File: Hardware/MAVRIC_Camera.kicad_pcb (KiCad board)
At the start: 2 copper layers, 7 parts, among them J1 MASTER, J2 CAMERA, J3 SERVO

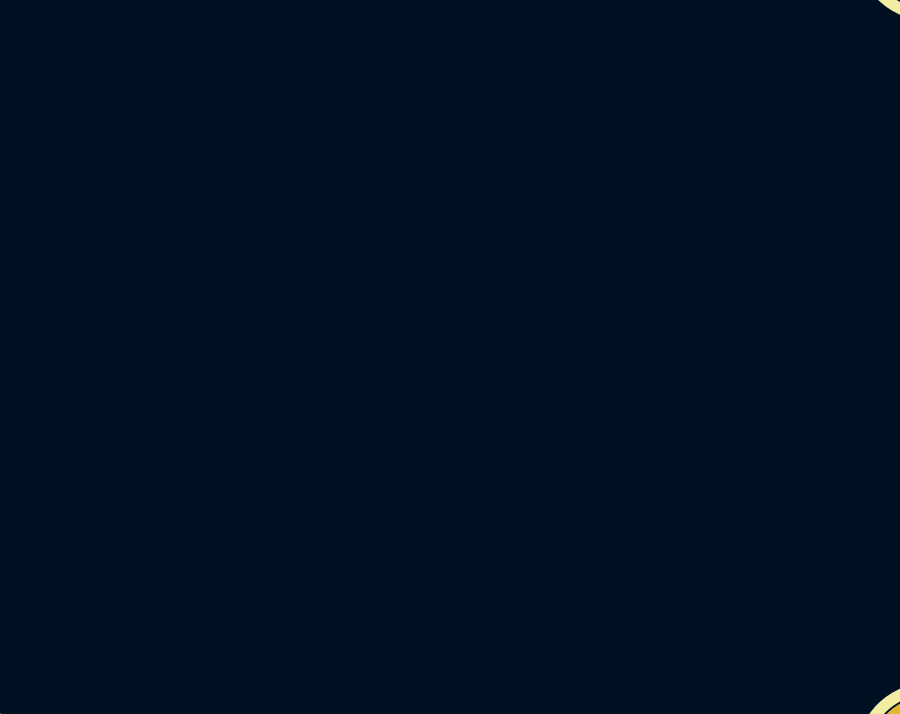
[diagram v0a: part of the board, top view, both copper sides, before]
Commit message: Add Dynamixel servo interface
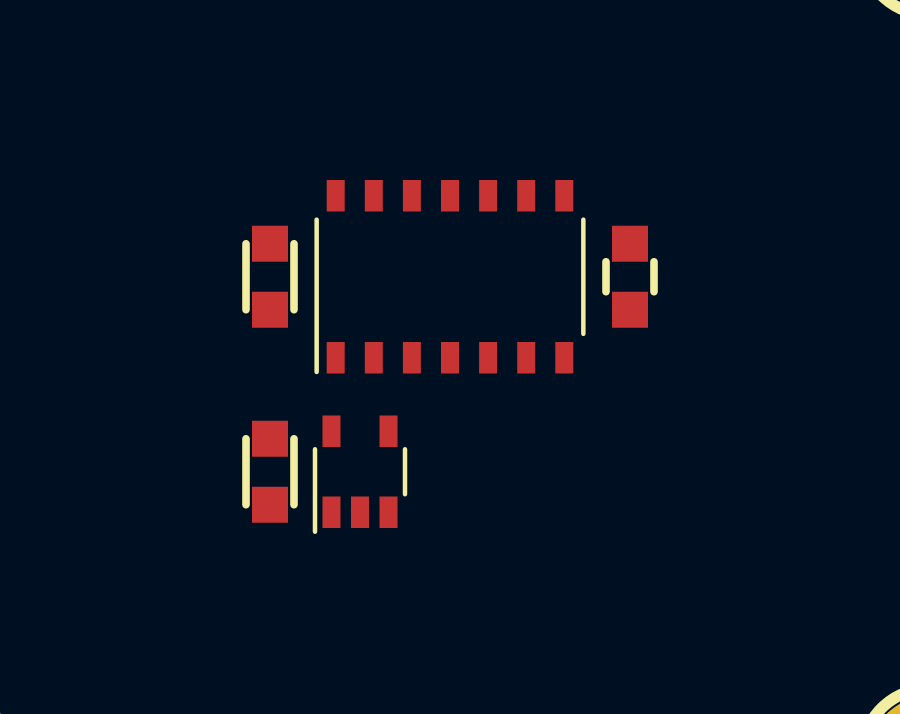
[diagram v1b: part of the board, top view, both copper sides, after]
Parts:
- added C1: 0.1uF, CAPC2012, F.Cu at (161.0, 111.0)
- added C2: 0.1uF, CAPC2012, F.Cu at (161.0, 117.5)
- added R1: 10k, RESC2012, F.Cu at (173.0, 111.0)
- added U1: SN74HC126, SOIC127P600-14N, F.Cu at (167.0, 111.0)
- added U2: SN74LVC1G04, SOT95P280-5N, F.Cu at (164.0, 117.5)
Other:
- net class Default: clearance 0.254 -> 0.2032; trace_width 0.254 -> 0.2032
- rule trace_clearance: 0.254 -> 0.2032
- rule trace_min: 0.254 -> 0.2032
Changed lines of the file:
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@@
 (kicad_pcb (version 3) (host pcbnew "(2013-07-07 BZR 4022)-stable")
   (general
-    (links 0)
-    (no_connects 0)
-    (area 147.269499 88.399999 217.244501 138.600001)
+    (links 11)
+    (no_connects 11)
+    (area 0 0 0 0)
     (thickness 1.6)
     (drawings 1)
     (tracks 0)
     (zones 0)
-    (modules 7)
-    (nets 1)
+    (modules 12)
+    (nets 6)
   )
   (page A3)
@@
   )
   (setup
-    (last_trace_width 0.254)
-    (trace_clearance 0.254)
+    (last_trace_width 0.2032)
+    (trace_clearance 0.2032)
     (zone_clearance 0.508)
     (zone_45_only no)
-    (trace_min 0.254)
+    (trace_min 0.2032)
     (segment_width 0.2)
     (edge_width 0.1)
@@
     (mod_text_size 1 1)
     (mod_text_width 0.15)
-    (pad_size 3.23 2.7)
+    (pad_size 0.6 1.05)
     (pad_drill 0)
     (pad_to_mask_clearance 0)
@@
   )
   (net 0 "")
+  (net 1 +5V)
+  (net 2 /SerDat)
+  (net 3 /SevDr)
+  (net 4 GND)
+  (net 5 N-000007)
   (net_class Default "This is the default net class."
-    (clearance 0.254)
-    (trace_width 0.254)
+    (clearance 0.2032)
+    (trace_width 0.2032)
     (via_dia 0.889)
     (via_drill 0.635)
@@
     (uvia_drill 0.127)
     (add_net "")
+    (add_net +5V)
+    (add_net /SerDat)
+    (add_net /SevDr)
+    (add_net GND)
+    (add_net N-000007)
   )
   (module 1pin (layer F.Cu)
@@
     )
   )
+  (module RESC2012 (layer F.Cu)
+    (at 173 111 90)
+    (fp_text reference R1 (at 0 0 180) (layer F.SilkS) hide
+      (effects (font (size 1.524 1.524) (thickness 0.3048)))
+    )
+    (fp_text value 10k (at 0 2.1 90) (layer F.SilkS) hide
+      (effects (font (size 1.524 1.524) (thickness 0.3048)))
+    )
+    (fp_line (start -0.5 0.8) (end 0.5 0.8) (layer F.SilkS) (width 0.254))
+    (fp_line (start -0.5 -0.8) (end 0.5 -0.8) (layer F.SilkS) (width 0.254))
+    (pad 1 smd rect (at -1.1 0 90) (size 1.2 1.2)
+      (layers F.Cu F.Paste F.Mask)
+      (net 2 /SerDat)
+    )
+    (pad 2 smd rect (at 1.1 0 90) (size 1.2 1.2)
+      (layers F.Cu F.Paste F.Mask)
+      (net 1 +5V)
+    )
+  )
+  (module CAPC2012 (layer F.Cu)
+    (at 161 111 270)
+    (descr "Cap 0805e / 2012m")
+    (fp_text reference C1 (at 0 0 360) (layer F.SilkS) hide
+      (effects (font (size 1.524 1.524) (thickness 0.3048)))
+    )
+    (fp_text value 0.1uF (at 0 2.1 270) (layer F.SilkS) hide
+      (effects (font (size 1.524 1.524) (thickness 0.3048)))
+    )
+    (fp_line (start 1.1 -0.8) (end -1.1 -0.8) (layer F.SilkS) (width 0.254))
+    (fp_line (start -1.1 0.8) (end 1.1 0.8) (layer F.SilkS) (width 0.254))
+    (pad 1 smd rect (at -1.1 0 270) (size 1.2 1.2)
+      (layers F.Cu F.Paste F.Mask)
+      (net 1 +5V)
+    )
+    (pad 2 smd rect (at 1.1 0 270) (size 1.2 1.2)
+      (layers F.Cu F.Paste F.Mask)
+      (net 4 GND)
+    )
+  )
+  (module SOT95P280-5N (layer F.Cu)
+    (at 164 117.5)
+    (fp_text reference U2 (at 0 0) (layer F.SilkS) hide
+      (effects (font (size 1 1) (thickness 0.15)))
+    )
+    (fp_text value SN74LVC1G04 (at 2.25 0 90) (layer F.SilkS) hide
+      (effects (font (size 1 1) (thickness 0.15)))
+    )
+    (fp_line (start 1.5 -0.75) (end 1.5 0.75) (layer F.SilkS) (width 0.15))
+    (fp_line (start -1.5 -0.75) (end -1.5 2) (layer F.SilkS) (width 0.15))
+    (pad 1 smd rect (at -0.95 1.35) (size 0.6 1.05)
+      (layers F.Cu F.Paste F.Mask)
+    )
+    (pad 2 smd rect (at 0 1.35) (size 0.6 1.05)
+      (layers F.Cu F.Paste F.Mask)
+      (net 3 /SevDr)
+    )
+    (pad 3 smd rect (at 0.95 1.35) (size 0.6 1.05)
+      (layers F.Cu F.Paste F.Mask)
+      (net 4 GND)
+    )
+    (pad 4 smd rect (at 0.95 -1.35) (size 0.6 1.05)
+      (layers F.Cu F.Paste F.Mask)
+      (net 5 N-000007)
+    )
+    (pad 5 smd rect (at -0.95 -1.35) (size 0.6 1.05)
+      (layers F.Cu F.Paste F.Mask)
+      (net 1 +5V)
+    )
+  )
+  (module CAPC2012 (layer F.Cu)
+    (at 161 117.5 270)
+    (descr "Cap 0805e / 2012m")
+    (fp_text reference C2 (at 0 0 360) (layer F.SilkS) hide
+      (effects (font (size 1.524 1.524) (thickness 0.3048)))
+    )
+    (fp_text value 0.1uF (at 0 2.1 270) (layer F.SilkS) hide
+      (effects (font (size 1.524 1.524) (thickness 0.3048)))
+    )
+    (fp_line (start 1.1 -0.8) (end -1.1 -0.8) (layer F.SilkS) (width 0.254))
+    (fp_line (start -1.1 0.8) (end 1.1 0.8) (layer F.SilkS) (width 0.254))
+    (pad 1 smd rect (at -1.1 0 270) (size 1.2 1.2)
+      (layers F.Cu F.Paste F.Mask)
+      (net 1 +5V)
+    )
+    (pad 2 smd rect (at 1.1 0 270) (size 1.2 1.2)
+      (layers F.Cu F.Paste F.Mask)
+      (net 4 GND)
+    )
+  )
+  (module SOIC127P600-14N (layer F.Cu)
+    (at 167 111)
+    (fp_text reference U1 (at 0 0) (layer F.SilkS) hide
+      (effects (font (size 1 1) (thickness 0.15)))
+    )
+    (fp_text value SN74HC126 (at 5.715 0 90) (layer F.SilkS) hide
+      (effects (font (size 1 1) (thickness 0.15)))
+    )
+    (fp_line (start 4.445 -1.905) (end 4.445 1.905) (layer F.SilkS) (width 0.15))
+    (fp_line (start -4.445 -1.905) (end -4.445 3.175) (layer F.SilkS) (width 0.15))
+    (pad 1 smd rect (at -3.81 2.7) (size 0.6 1.05)
+      (layers F.Cu F.Paste F.Mask)
+      (net 3 /SevDr)
+    )
+    (pad 2 smd rect (at -2.54 2.7) (size 0.6 1.05)
+      (layers F.Cu F.Paste F.Mask)
+    )
+    (pad 3 smd rect (at -1.27 2.7) (size 0.6 1.05)
+      (layers F.Cu F.Paste F.Mask)
+      (net 2 /SerDat)
+    )
+    (pad 4 smd rect (at 0 2.7) (size 0.6 1.05)
+      (layers F.Cu F.Paste F.Mask)
+      (net 5 N-000007)
+    )
+    (pad 5 smd rect (at 1.27 2.7) (size 0.6 1.05)
+      (layers F.Cu F.Paste F.Mask)
+      (net 2 /SerDat)
+    )
+    (pad 6 smd rect (at 2.54 2.7) (size 0.6 1.05)
+      (layers F.Cu F.Paste F.Mask)
+    )
+    (pad 7 smd rect (at 3.81 2.7) (size 0.6 1.05)
+      (layers F.Cu F.Paste F.Mask)
+      (net 4 GND)
+    )
+    (pad 8 smd rect (at 3.81 -2.7) (size 0.6 1.05)
+      (layers F.Cu F.Paste F.Mask)
+    )
+    (pad 9 smd rect (at 2.54 -2.7) (size 0.6 1.05)
+      (layers F.Cu F.Paste F.Mask)
+    )
+    (pad 10 smd rect (at 1.27 -2.7) (size 0.6 1.05)
+      (layers F.Cu F.Paste F.Mask)
+    )
+    (pad 11 smd rect (at 0 -2.7) (size 0.6 1.05)
+      (layers F.Cu F.Paste F.Mask)
+    )
+    (pad 12 smd rect (at -1.27 -2.7) (size 0.6 1.05)
+      (layers F.Cu F.Paste F.Mask)
+    )
+    (pad 13 smd rect (at -2.54 -2.7) (size 0.6 1.05)
+      (layers F.Cu F.Paste F.Mask)
+    )
+    (pad 14 smd rect (at -3.81 -2.7) (size 0.6 1.05)
+      (layers F.Cu F.Paste F.Mask)
+      (net 1 +5V)
+    )
+  )

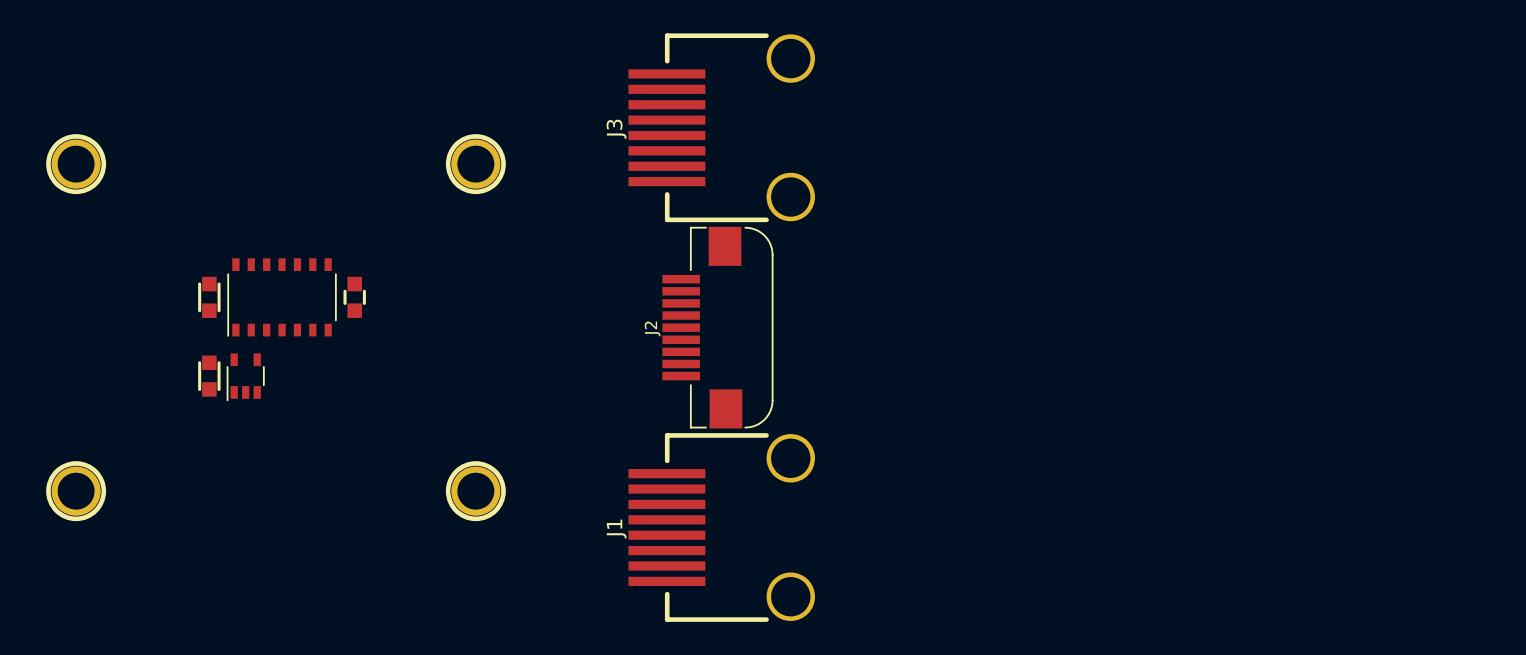
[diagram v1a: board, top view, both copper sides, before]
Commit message: Add servo power supply.
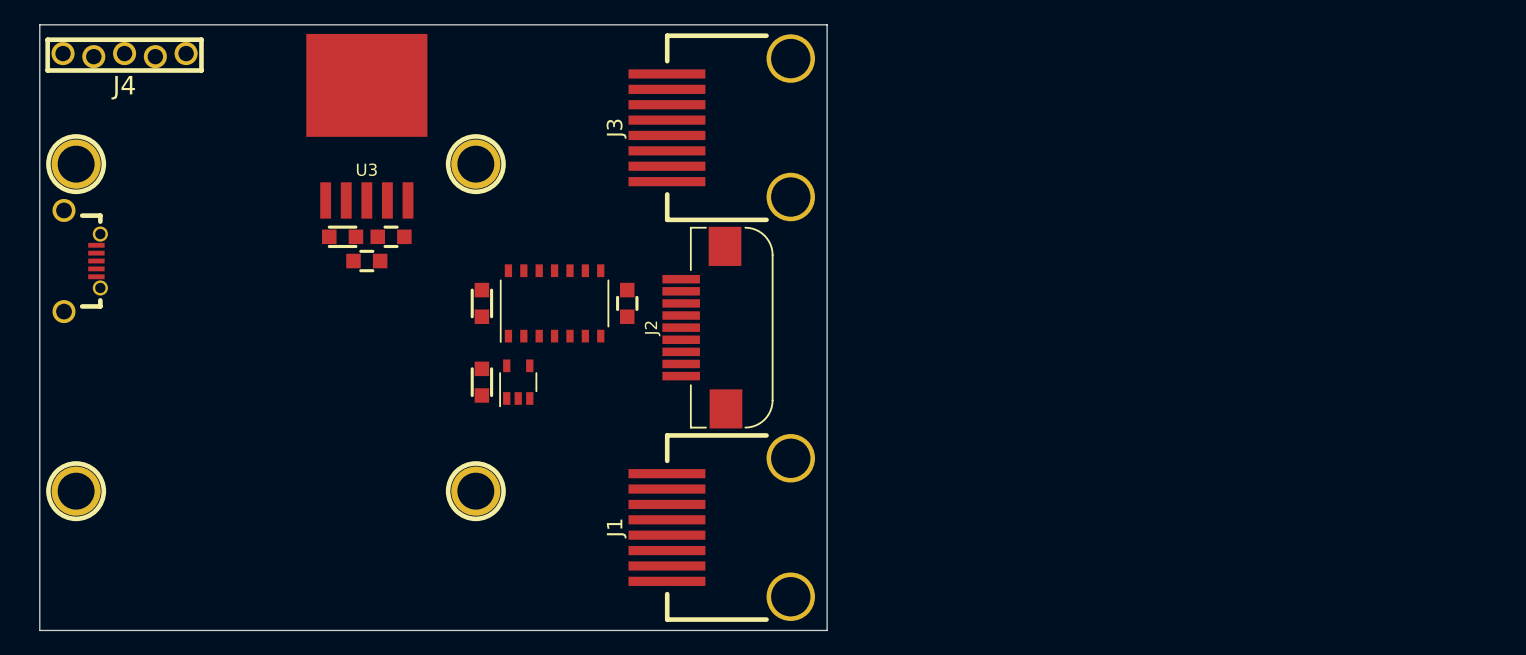
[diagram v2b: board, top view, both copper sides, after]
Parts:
- added C4: C, CAPC2012, F.Cu at (172.0, 106.0)
- added J4: ICSP-PIC, HDRV5W38P254_5X1-LOCK, F.Cu at (154.0, 91.0)
- added J5: USB, WM17143CT, F.Cu at (149.0, 108.0)
- added R2: R, RESC2012, F.Cu at (176.0, 106.0)
- added R3: R, RESC2012, F.Cu at (174.0, 108.0)
- added U3: BA00DD0W, TO263-6N, F.Cu at (174.0, 103.0)
- moved C1 22.5 mm to (183.5, 111.5)
- moved C2 22.5 mm to (183.5, 118.0)
- moved R1 22.5 mm to (195.5, 111.5)
- moved U1 22.5 mm to (189.5, 111.5)
- moved U2 22.5 mm to (186.5, 118.0)
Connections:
- J1 pad 4: (no net) -> +BATT
- J1 pad 5: (no net) -> +BATT
- J1 pad 7: (no net) -> GND
- J1 pad 8: (no net) -> GND
- J2 pad 3: (no net) -> GND
- J2 pad 5: (no net) -> GND
- J2 pad 7: (no net) -> GND
- J2 pad 9: (no net) -> GND
- J3 pad 1: (no net) -> /SevDat
- J3 pad 2: (no net) -> GND
- J3 pad 3: (no net) -> N-0000014
- J3 pad 4: (no net) -> N-0000014
- J3 pad 5: (no net) -> N-0000014
- J3 pad 6: (no net) -> N-0000014
- J3 pad 7: (no net) -> GND
- J3 pad 8: (no net) -> GND
- R1 pad 1: /SerDat -> /SevDat
- U1 pad 3: /SerDat -> /SevDat
- U1 pad 5: /SerDat -> /SevDat
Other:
- board outline added: 65 x 50 mm

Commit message: Remove dynamixel interface, Add standard PWM
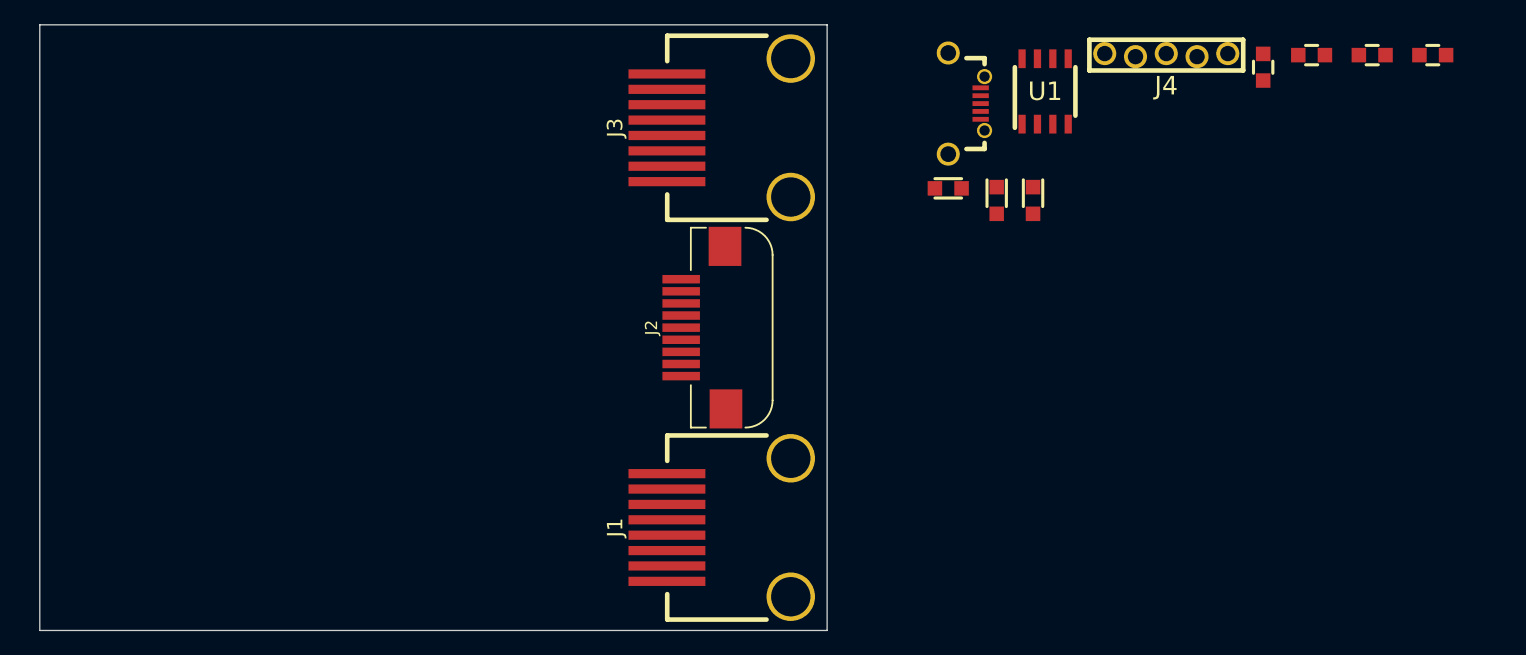
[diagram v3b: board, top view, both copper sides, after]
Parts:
- removed 1PIN (x4): P***, 1pin
- removed C4: C, CAPC2012
- removed U2: SN74LVC1G04, SOT95P280-5N
- removed U3: BA00DD0W, TO263-6N
- added C3: C, CAPC2012, F.Cu at (222.0, 102.0)
- added R4: R, RESC2012, F.Cu at (262.0, 91.0)
- C1, C2: value 0.1uF -> CP; footprint CAPC2012 -> CAPCP2012
- R1: value 10k -> R
- U1: value SN74HC126 -> AOZ1031; footprint SOIC127P600-14N -> SOIC127P600X175-8N
- moved J4 86.0 mm to (240.0, 91.0)
- moved R3 84.7 mm to (257.0, 91.0)
- moved R2 77.5 mm to (252.0, 91.0)
- moved J5 74.1 mm to (222.0, 95.0)
- moved R1 56.0 mm to (248.0, 92.0)
- moved C2 47.9 mm to (229.0, 103.0)
- moved U1 44.1 mm to (230.0, 94.0)
- moved C1 43.3 mm to (226.0, 103.0)
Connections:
- C1 pad 1: +5V -> N-000004
- C2 pad 1: +5V -> +BATT
- J1 pad 1: (no net) -> /Video
- J1 pad 2: (no net) -> GND
- J2 pad 6: (no net) -> /Video
- J3 pad 1: /SevDat -> (no net)
- J3 pad 3: N-0000014 -> (no net)
- J3 pad 4: N-0000014 -> N-000004
- J3 pad 5: N-0000014 -> N-000004
- J3 pad 6: N-0000014 -> GND
- R1 pad 1: /SevDat -> N-000003
- R1 pad 2: +5V -> N-000004
- R2 pad 1: N-0000015 -> GND
- R2 pad 2: N-0000014 -> /ServoEn
- R3 pad 1: GND -> N-000002
- R3 pad 2: N-0000015 -> N-000001
- U1 pad 1: /SevDr -> GND
- U1 pad 2: (no net) -> +BATT
- U1 pad 3: /SevDat -> GND
- U1 pad 4: N-0000010 -> N-000003
- U1 pad 5: /SevDat -> N-000001
- U1 pad 6: (no net) -> /ServoEn
- U1 pad 7: GND -> N-000004
- U1 pad 8: (no net) -> N-000004
